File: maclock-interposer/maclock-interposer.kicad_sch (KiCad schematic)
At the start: 3 parts, among them J1 HC-PM254-8.5H-2x20PS, J2 PZ254V-11-07P, J3 HB-PH9-254220PB2GOP

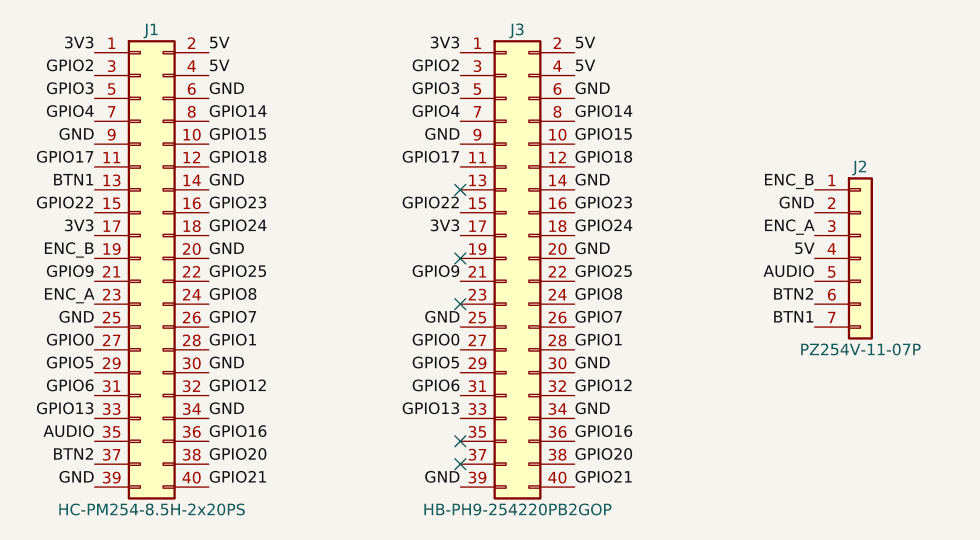
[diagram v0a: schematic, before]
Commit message: Interposer J2: female socket on the screen side, 1.5 mm further south
The cable now plugs in from the screen side, so J2 is a 1x7 female
socket (XFCN PM254V-11-07-H85, LCSC C2832270) on top, in the same pin
order. The board grows 1.5 mm south to make room, and J2's labels move
to both sides and read "Dial A" / "Dial B" like the breakout's. ENC_A
and BTN2 are re-routed so the screen-side lettering sits on unbroken
silk. Schematic fields carry manufacturer, MPN and LCSC for all three
connectors.
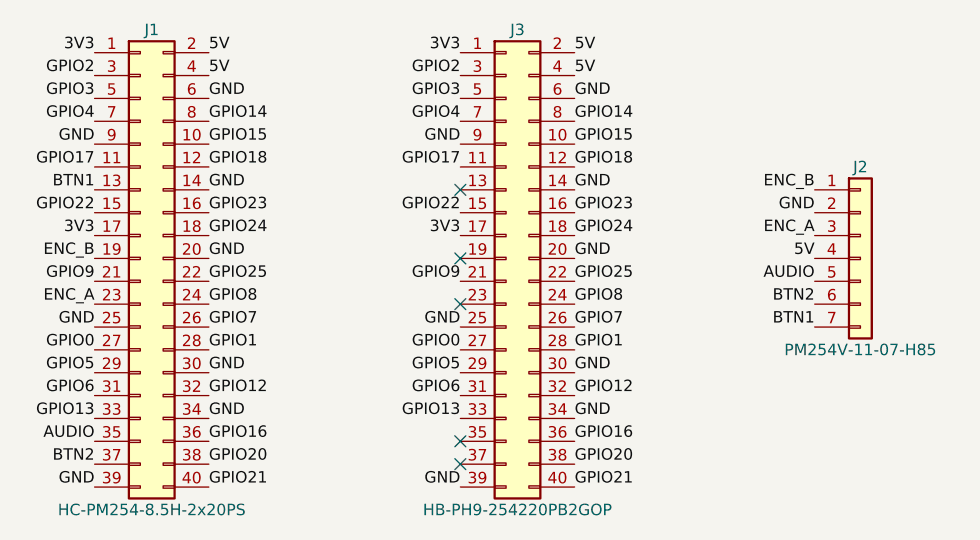
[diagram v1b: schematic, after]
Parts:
- J1: LCSC (none) -> C22436166; MPN (none) -> HC-PM254-8.5H-2x20PS; Manufacturer (none) -> Hong Cheng
- J2: value PZ254V-11-07P -> PM254V-11-07-H85; footprint Connector_PinHeader_2.54mm:PinHeader_1x07_P2.54mm_Vertical -> Connector_PinSocket_2.54mm:PinSocket_1x07_P2.54mm_Vertical; LCSC (none) -> C2832270; MPN (none) -> PM254V-11-07-H85; Manufacturer (none) -> XFCN
- J3: LCSC (none) -> C6332245; MPN (none) -> HB-PH9-254220PB2GOP; Manufacturer (none) -> Hanbo Electronic
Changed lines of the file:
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@@
+			)
+		)
+		(property "Manufacturer" "Hong Cheng"
+			(at 100.33 100.33 0)
+			(hide yes)
+			(effects
+				(font
+					(size 1.27 1.27)
+				)
+			)
+		)
+		(property "MPN" "HC-PM254-8.5H-2x20PS"
+			(at 100.33 100.33 0)
+			(hide yes)
+			(effects
+				(font
+					(size 1.27 1.27)
+				)
+			)
+		)
+		(property "LCSC" "C22436166"
+			(at 100.33 100.33 0)
+			(hide yes)
+			(effects
+				(font
+					(size 1.27 1.27)
+				)
 			)
 		)
@@
 			)
 		)
-		(property "Value" "PZ254V-11-07P"
+		(property "Value" "PM254V-11-07-H85"
 			(at 180.34 110.49 0)
 			(effects
@@
 			)
 		)
-		(property "Footprint" "Connector_PinHeader_2.54mm:PinHeader_1x07_P2.54mm_Vertical"
+		(property "Footprint" "Connector_PinSocket_2.54mm:PinSocket_1x07_P2.54mm_Vertical"
 			(at 180.34 100.33 0)
 			(hide yes)
@@
 			)
 		)
-		(property "Datasheet" ""
+		(property "Datasheet" "https://www.lcsc.com/product-detail/C2832270.html"
 			(at 180.34 100.33 0)
 			(hide yes)
@@
 			)
 		)
-		(property "Description" "Generic connector, single row, 01x07, script generated (kicad-library-utils/schlib/autogen/connector/)"
+		(property "Description" "1x7 female header (socket), 2.54 mm, 8.5 mm, through-hole"
+			(at 180.34 100.33 0)
+			(hide yes)
+			(effects
+				(font
+					(size 1.27 1.27)
+				)
+			)
+		)
+		(property "Manufacturer" "XFCN"
+			(at 180.34 100.33 0)
+			(hide yes)
+			(effects
+				(font
+					(size 1.27 1.27)
+				)
+			)
+		)
+		(property "MPN" "PM254V-11-07-H85"
+			(at 180.34 100.33 0)
+			(hide yes)
+			(effects
+				(font
+					(size 1.27 1.27)
+				)
+			)
+		)
+		(property "LCSC" "C2832270"
 			(at 180.34 100.33 0)
 			(hide yes)
@@
 			(at 140.97 100.33 0)
 			(hide yes)
+			(effects
+				(font
+					(size 1.27 1.27)
+				)
+			)
+		)
+		(property "Manufacturer" "Hanbo Electronic"
+			(at 140.97 100.33 0)
+			(hide yes)
+			(effects
+				(font
+					(size 1.27 1.27)
+				)
+			)
+		)
+		(property "MPN" "HB-PH9-254220PB2GOP"
+			(at 140.97 100.33 0)
+			(hide yes)
+			(effects
+				(font
+					(size 1.27 1.27)
+				)
+			)
+		)
+		(property "LCSC" "C6332245"
+			(at 140.97 100.33 0)
+			(hide yes)
